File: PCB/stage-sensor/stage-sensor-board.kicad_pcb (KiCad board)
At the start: 2 copper layers, 19.4 x 19.4 mm, 11 parts, among them J1 STEMMA QT, U1 ICM 42605, U3 SHT45

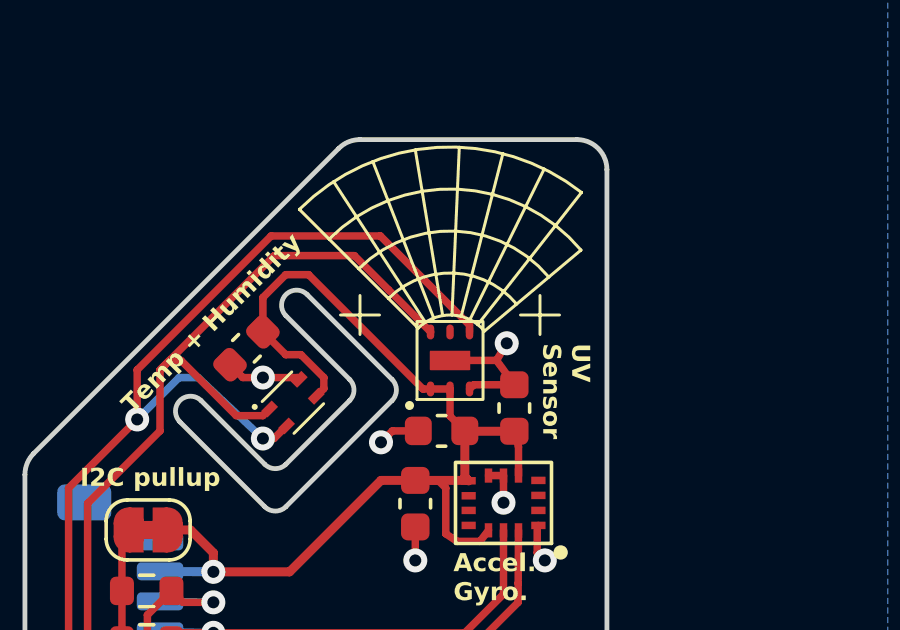
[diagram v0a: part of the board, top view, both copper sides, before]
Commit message: Update PCB files
Pre-removal and submodule reorganisation
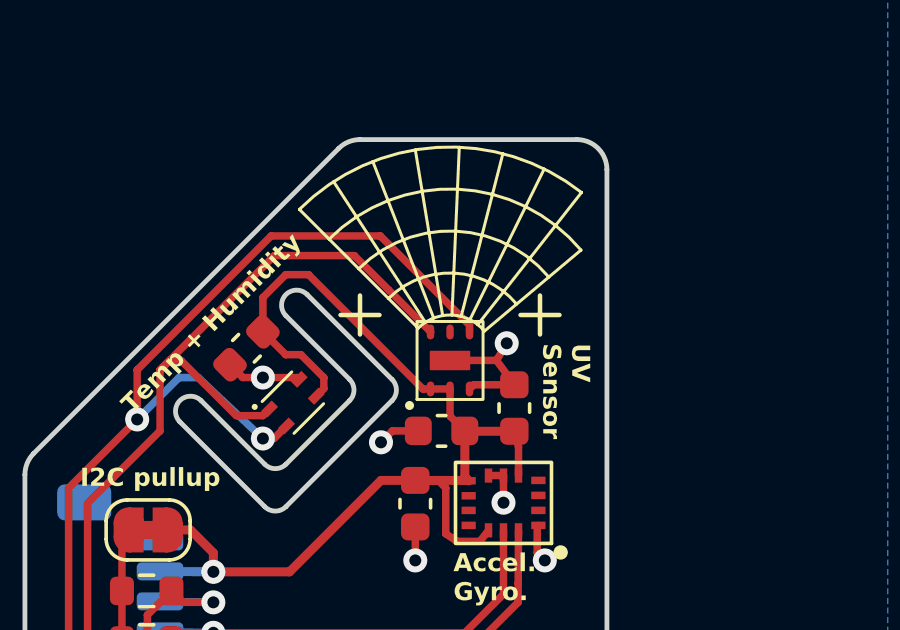
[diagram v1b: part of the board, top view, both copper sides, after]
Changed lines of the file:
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@@
     (stroke (width 0.1) (type solid)) (layer "F.SilkS"))
   (gr_line (start 142.206 88.832) (end 142.206 90.132)
-    (stroke (width 0.1) (type solid)) (layer "F.SilkS"))
+    (stroke (width 0.15) (type solid)) (layer "F.SilkS"))
   (gr_arc (start 136.165441 87.941441) (mid 139.393727 86.6861) (end 142.500201 88.218264)
     (stroke (width 0.1) (type solid)) (layer "F.SilkS"))
@@
     (stroke (width 0.1) (type solid)) (layer "F.SilkS"))
   (gr_line (start 135.556 89.482) (end 136.856 89.482)
-    (stroke (width 0.1) (type solid)) (layer "F.SilkS"))
+    (stroke (width 0.15) (type solid)) (layer "F.SilkS"))
   (gr_line (start 141.556 89.482) (end 142.856 89.482)
-    (stroke (width 0.1) (type solid)) (layer "F.SilkS"))
+    (stroke (width 0.15) (type solid)) (layer "F.SilkS"))
   (gr_line (start 136.206 90.132) (end 136.206 88.832)
-    (stroke (width 0.1) (type solid)) (layer "F.SilkS"))
+    (stroke (width 0.15) (type solid)) (layer "F.SilkS"))
   (gr_line (start 139.57847 89.52898) (end 140.969024 84.104374)
     (stroke (width 0.1) (type solid)) (layer "F.SilkS"))
